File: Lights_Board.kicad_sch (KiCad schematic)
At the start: 72 parts, among them J1 Conn_ARM_JTAG_SWD_10, J2 USB_B_Micro, J3 34830-0801, J6 34830-0801, J7 34830-0801, J8 34830-0801, Q1 AO3400A, Q2 AO3400A, Q3 AO3400A, Q4 AO3400A, Q5 AO3400A, Q6 AO3400A, Q7 AO4407A, Q8 IRFZ44NPBF, U1 STM32F072RBTx, U10 IR2104STRPBF, U2 TPS2113, U3 TCAN1042xV, U4 AMS1117-5.0, U6 LSM6DS3, U7 MCP33151, U8 MCP33151, U9 AMS1117

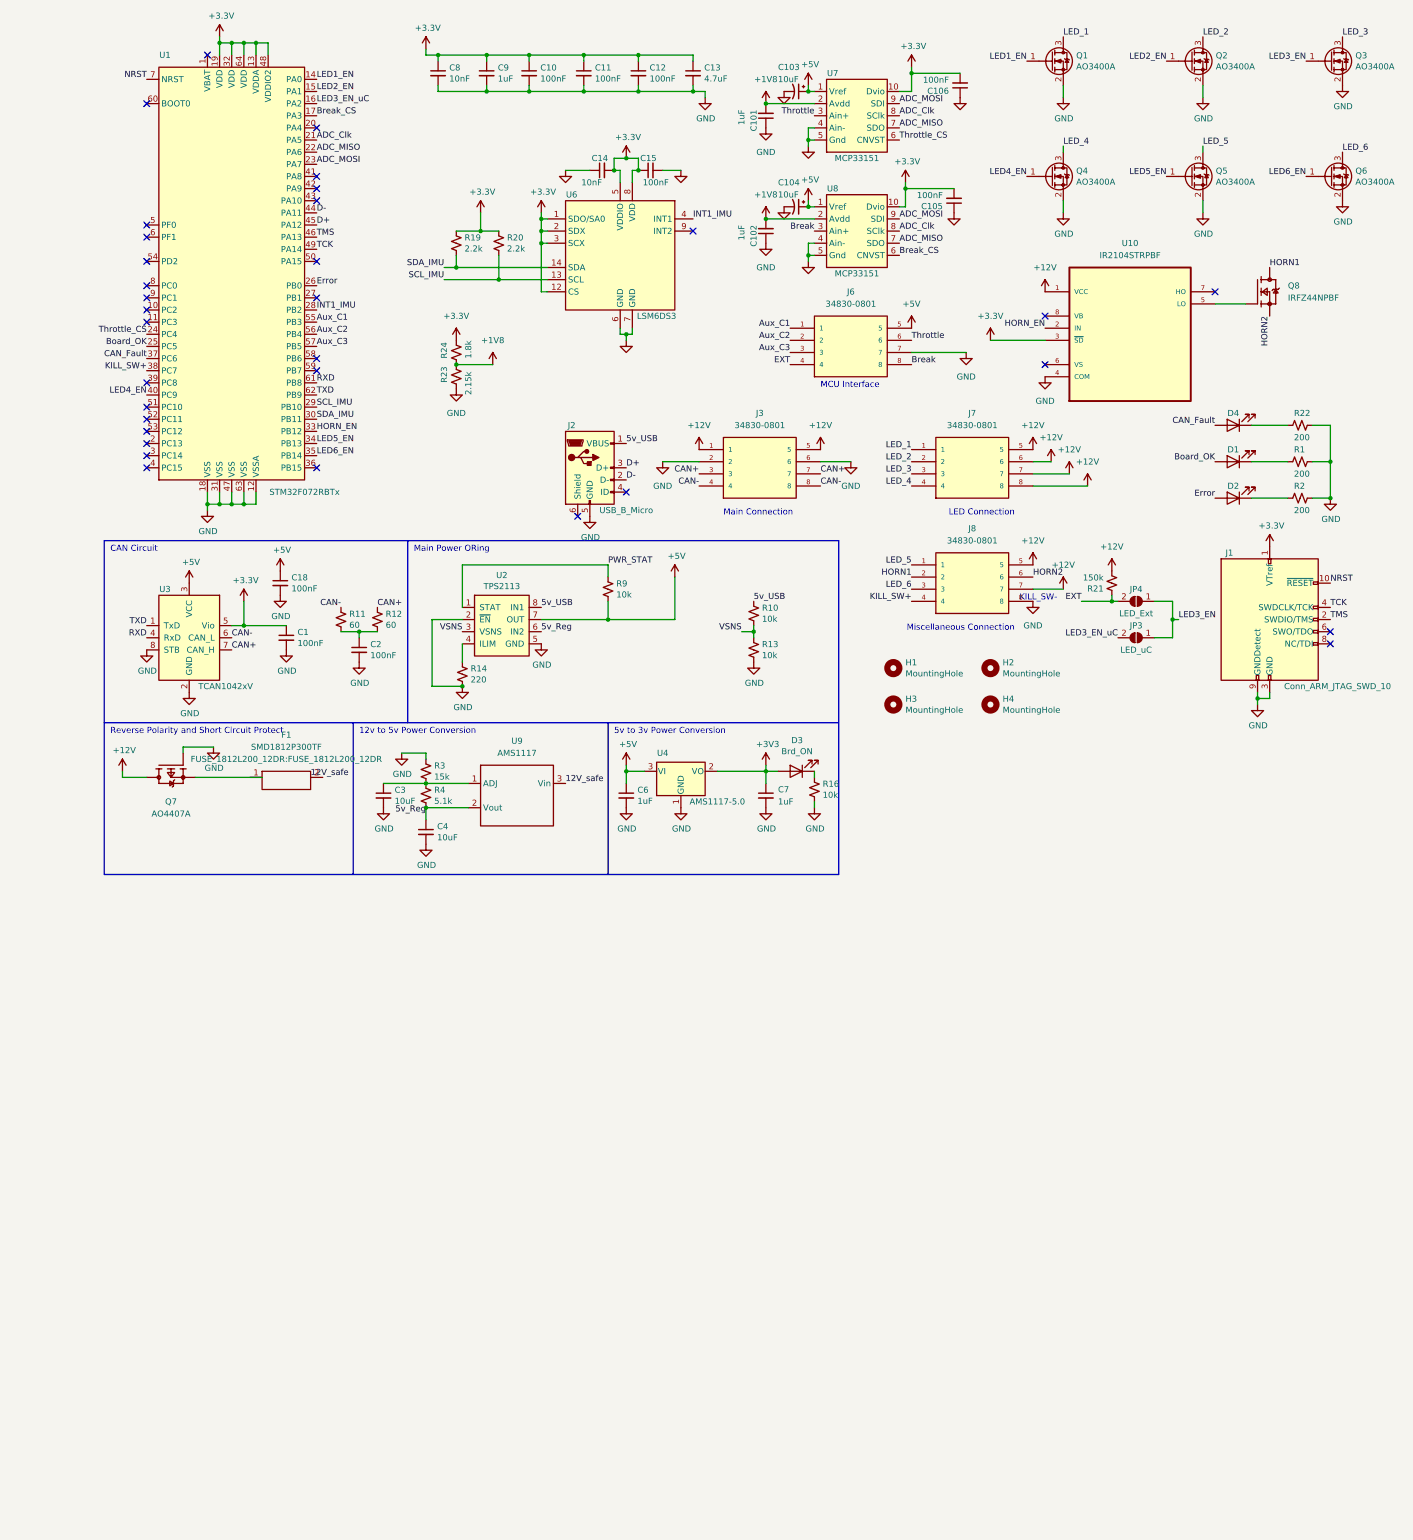
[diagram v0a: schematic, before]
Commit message: FSGP 2023 Lights Hardware
Final PCB revision used for Sunrider at FSGP 2023
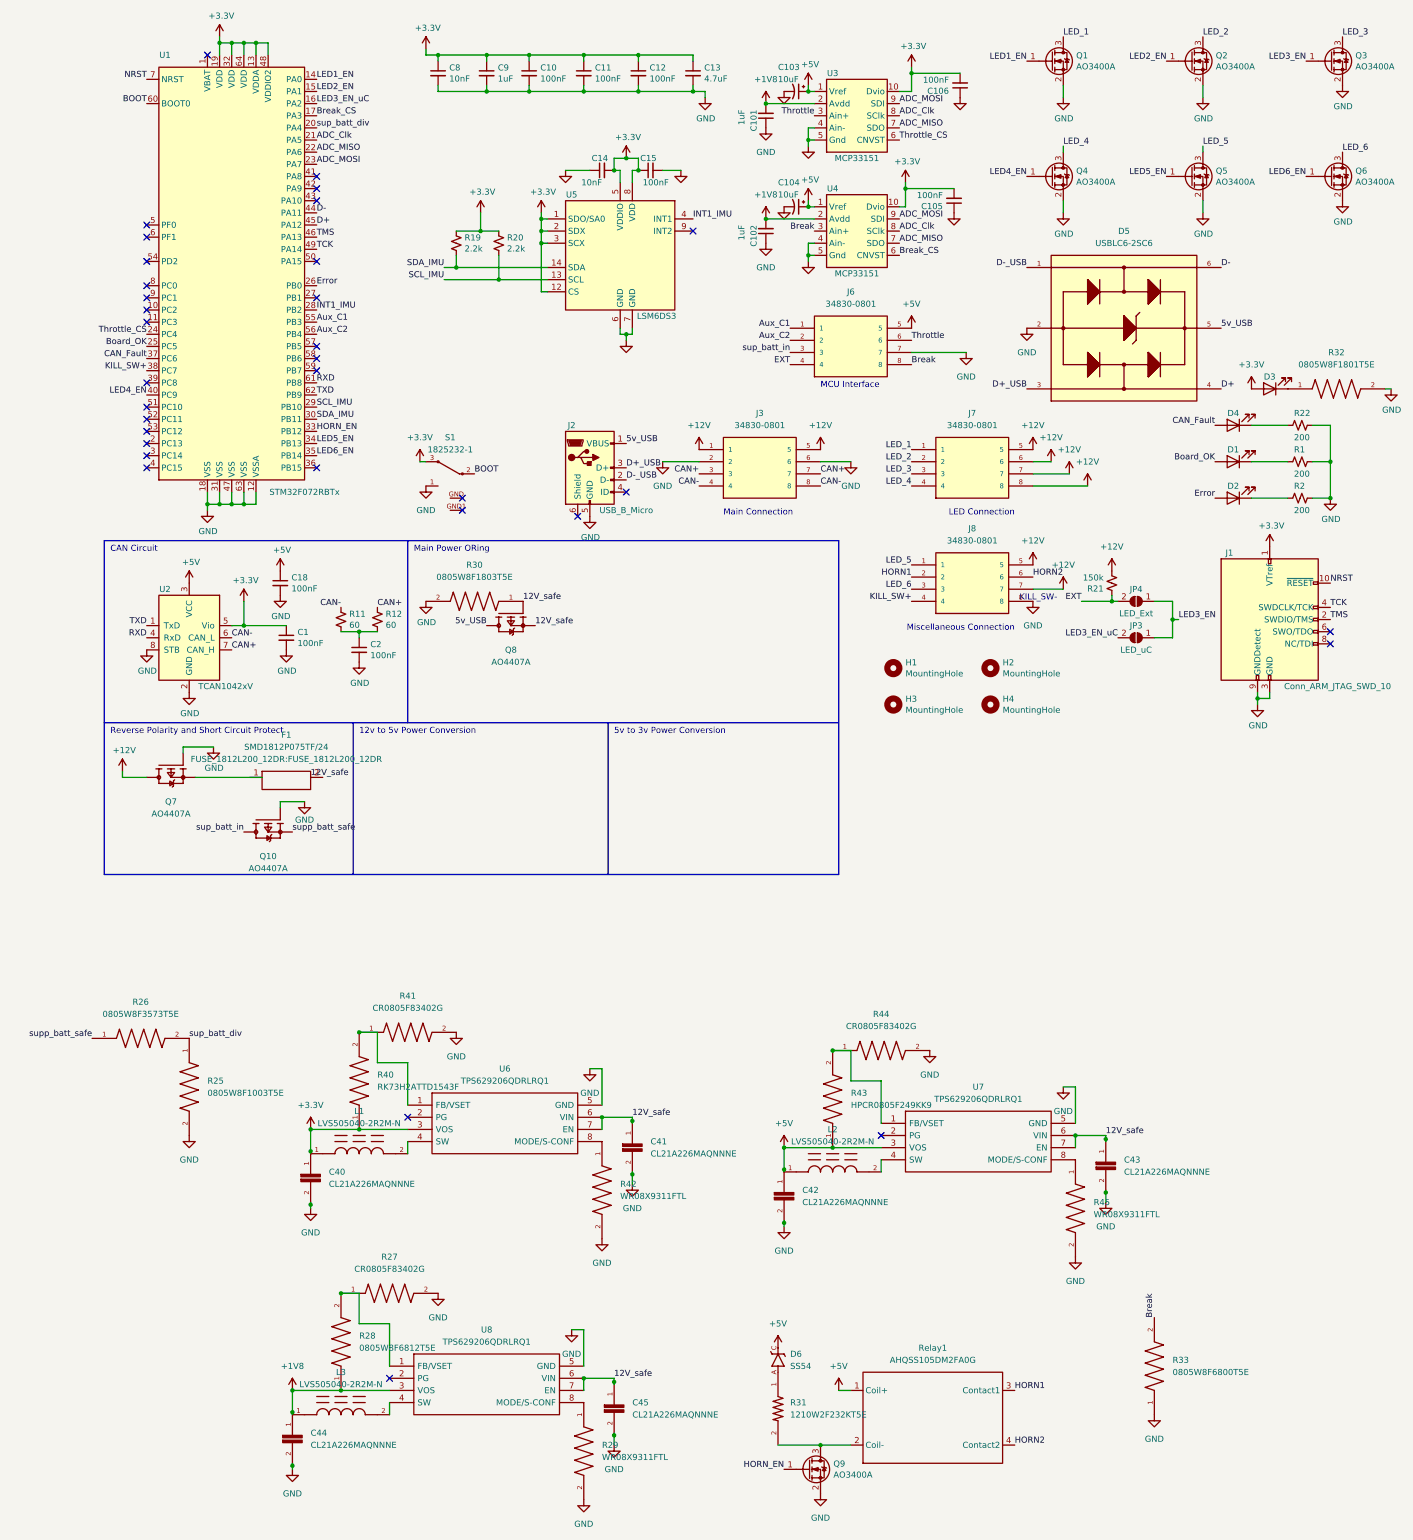
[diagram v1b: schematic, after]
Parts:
- removed C3, C4: 10uF, Capacitor_SMD:C_0402_1005Metric, symbol Device:C_Small
- removed C6, C7: 1uF, Capacitor_SMD:C_0402_1005Metric, symbol Device:C_Small
- removed Q8: IRFZ44NPBF, TO254P1016X419X2286-3, symbol IRFZ44NPBF:IRFZ44NPBF
- removed R10, R13, R16, R9: 10k, Resistor_SMD:R_0603_1608Metric, symbol Device:R_Small_US
- removed R14: 220, Resistor_SMD:R_0603_1608Metric, symbol Device:R_Small_US
- removed R23: 2.15k, Resistor_SMD:R_0603_1608Metric, symbol Device:R_Small_US
- removed R24: 1.8k, Resistor_SMD:R_0805_2012Metric, symbol Device:R_Small_US
- removed R3: 15k, Resistor_SMD:R_0603_1608Metric, symbol Device:R_Small_US
- removed R4: 5.1k, Resistor_SMD:R_0603_1608Metric, symbol Device:R_Small_US
- removed U10: IR2104STRPBF, SOIC127P600X175-8N, symbol IR2104STRPBF:IR2104STRPBF
- removed U2: TPS2113, Package_SO:TSSOP-8_4.4x3mm_P0.65mm, symbol JohnLib:TPS2113
- removed U4: AMS1117-5.0, Package_TO_SOT_SMD:SOT-223-3_TabPin2, symbol Regulator_Linear:AMS1117-5.0
- removed U9: AMS1117, AMS1117 (1):SOT229P700X180-4N, symbol New_Library:AMS1117
- added C40, C41, C42, C43, C44, C45: CL21A226MAQNNNE, CAPC2012X140N, symbol CL21A226MAQNNNE:CL21A226MAQNNNE
- added D5: USBLC6-2SC6, SOT95P280X145-6N, symbol USBLC6-2SC6:USBLC6-2SC6
- added D6: SS54, DO-214AC, symbol SS54:SS54
- added L1, L2, L3: LVS505040-2R2M-N, IND_SDR0403-2R2ML, symbol SDR0403-2R2ML:SDR0403-2R2ML
- added Q10, Q8: AO4407A, SOIC127P600X175-8N, symbol AO4407A:AO4407A
- added Q9: AO3400A, Package_TO_SOT_SMD:SOT-23, symbol Device:Q_NMOS_GSD
- added R25: 0805W8F1003T5E, RESC2012X60N, symbol CR0805AJ_-000EAS:CR0805AJ/-000EAS
- added R26: 0805W8F3573T5E, RESC2012X60N, symbol CR0805AJ_-000EAS:CR0805AJ/-000EAS
- added R27, R41, R44: CR0805F83402G, RESC2012X60N, symbol CR0805AJ_-000EAS:CR0805AJ/-000EAS
- added R28: 0805W8F6812T5E, RESC2012X60N, symbol CR0805AJ_-000EAS:CR0805AJ/-000EAS
- added R29, R42, R45: WR08X9311FTL, RESC2012X60N, symbol CR0805AJ_-000EAS:CR0805AJ/-000EAS
- added R30: 0805W8F1803T5E, RESC2012X60N, symbol CR0805AJ_-000EAS:CR0805AJ/-000EAS
- added R31: 1210W2F232KT5E, RESC3125X65N, symbol 3-1879463-6:3-1879463-6
- added R32: 0805W8F1801T5E, RESC2012X60N, symbol CR0805AJ_-000EAS:CR0805AJ/-000EAS
- added R33: 0805W8F6800T5E, RESC2012X60N, symbol CR0805AJ_-000EAS:CR0805AJ/-000EAS
- added R40: RK73H2ATTD1543F, RESC2012X60N, symbol CR0805AJ_-000EAS:CR0805AJ/-000EAS
- added R43: HPCR0805F249KK9, RESC2012X60N, symbol CR0805AJ_-000EAS:CR0805AJ/-000EAS
- added Relay1: AHQSS105DM2FA0G, FUSE_1812L200_12DR:AHQSS105DM2FA0G, symbol AHQSS105DM2FA0G:AHQSS105DM2FA0G
- added S1: 1825232-1, 1825232-1, symbol 1825232-1:1825232-1
- added U6, U7, U8: TPS629206QDRLRQ1, SOTFL50P160X60-8N, symbol SamacSys_Parts:TPS629206QDRLRQ1
- D3: value Brd_ON -> Board OK
- F1: value SMD1812P300TF -> SMD1812P075TF/24; JLCPCB (none) -> C12557
- U2: renamed from U3; footprint JohnLib:SOIC-8 -> TCAN1042VDQ1:SOIC127P599X175-8N
- renumbered U7 to U3, U8 to U4, U6 to U5
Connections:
- net +1V8: now also C44.1, L3.1, R28.1, U8.3 (VOS)
- net +3V3: now also C40.1, L1.1, R40.1, S1.3, U6.3 (VOS)
- net +5V: now also C42.1, D6.C, L2.1, R43.1, Relay1.1 (Coil+), U7.3 (VOS)
- net 12V_safe: now also C41.1, C43.1, C45.1, Q8.1, Q8.2, Q8.3, Q8.4, R30.1, U6.6 (VIN), U6.7 (EN), U7.6 (VIN), U7.7 (EN), U8.6 (VIN), U8.7 (EN)
- net 5v_USB: now also D5.5, Q8.5, Q8.6, Q8.7, Q8.8
- net Break: now also R33.2
- net D+: now also D5.4; no longer J2.3 (D+)
- net D-: now also D5.6; no longer J2.2 (D-)
- net GND: now also C40.2, C41.2, C42.2, C43.2, C44.2, C45.2, D5.2, Q10.4, Q9.2 (S), R25.2, R27.2, R29.2, R30.2, R32.2, R33.1, R41.2, R42.2, R44.2, R45.2, S1.1, U6.5 (GND), U7.5 (GND), U8.5 (GND)
- net HORN1: now also Relay1.3 (Contact1)
- net HORN2: now also Relay1.4 (Contact2)
- net HORN_EN: now also Q9.1 (G)
- net sup_batt_div: now reaches U1.20 (PA4)
- net sup_batt_div: now also R25.1, R26.2
- net BOOT: now reaches U1.60 (BOOT0)
- net BOOT: now also S1.2
- net at D3.1 (K): now also R32.1
- net Aux_C3: no longer names the net of U1.57 (PB5)
- net Aux_C3: no longer J6.3
- new net: R43.2, R44.1, U7.1 (FB/VSET)
- new net: L2.2, U7.4 (SW)
- new net: Q9.3 (D), R31.2, Relay1.2 (Coil-)
- new net: D6.A, R31.1
- new net: L3.2, U8.4 (SW)
- new net: R40.2, R41.1, U6.1 (FB/VSET)
- new net: R27.1, R28.2, U8.1 (FB/VSET)
- new net: R29.1, U8.8 (MODE/S-CONF)
- new net: R42.1, U6.8 (MODE/S-CONF)
- new net: L1.2, U6.4 (SW)
- new net: R45.1, U7.8 (MODE/S-CONF)
- new net D+_USB: D5.3, J2.3 (D+)
- new net D-_USB: D5.1, J2.2 (D-)
- new net sup_batt_in: J6.3, Q10.5, Q10.6, Q10.7, Q10.8
- new net supp_batt_safe: Q10.1, Q10.2, Q10.3, R26.1
- no-connect marks 33 -> 34
